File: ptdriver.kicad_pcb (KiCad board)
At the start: 2 copper layers, 100 x 50 mm, 66 parts, among them J1 Power, J10 Heaters, J2 Vout, J3 serial port, J4 3-wire PT100 probe, J5 Conn_01x02, J6 Conn_02x03_Odd_Even, J7 display, J8 3-wire PT100 probe, J9 Vout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

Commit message: Re-arrange and rename things to survive a move from one folder to another
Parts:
- added G***: LOGO, weo_footprints:mit_logo, F.Cu at (112.8, 123.2)
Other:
- board text added: "MAX31865"
- board text added: "© Metamachine 2021"
- board text removed: "Metamachine 9/8/2021"

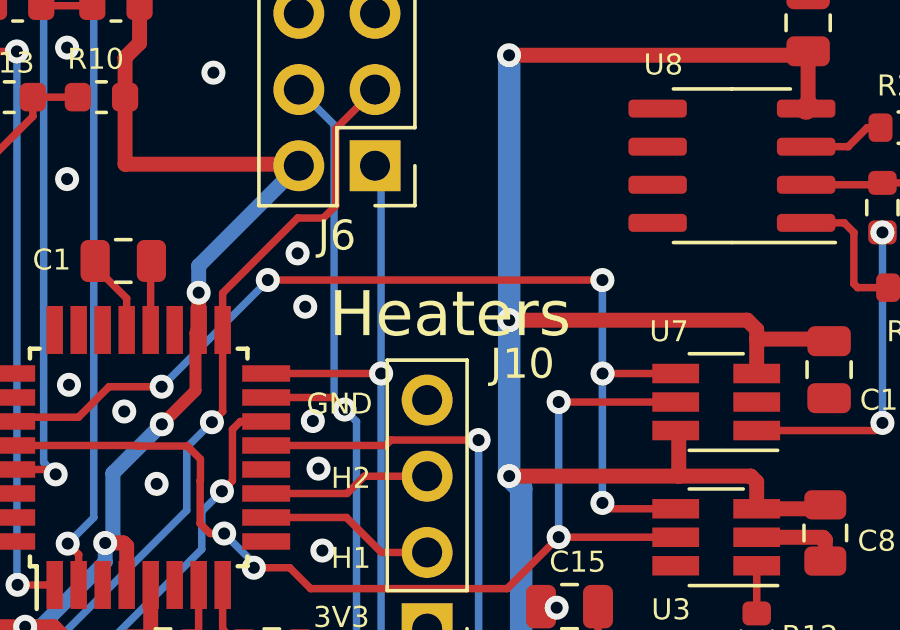
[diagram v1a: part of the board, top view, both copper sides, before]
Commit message: Update picture of board; Fix a couple of windy traces
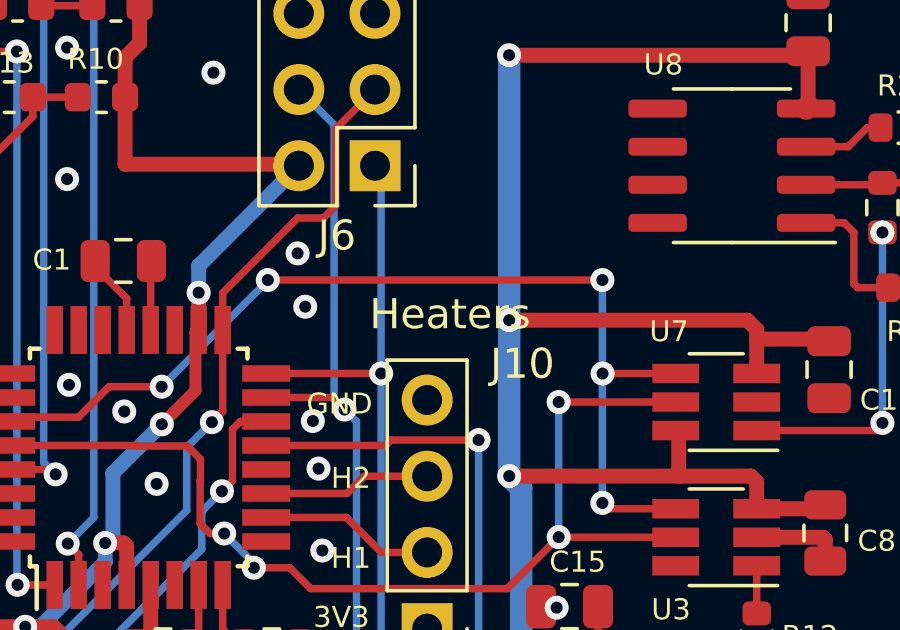
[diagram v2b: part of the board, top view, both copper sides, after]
